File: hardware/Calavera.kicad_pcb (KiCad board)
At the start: 2 copper layers, 39.2 x 59.2 mm, 24 parts, among them Q1 DMN65D8L, SW1 SW_SPDT, U1 AT42QT1012, U2 LMV932

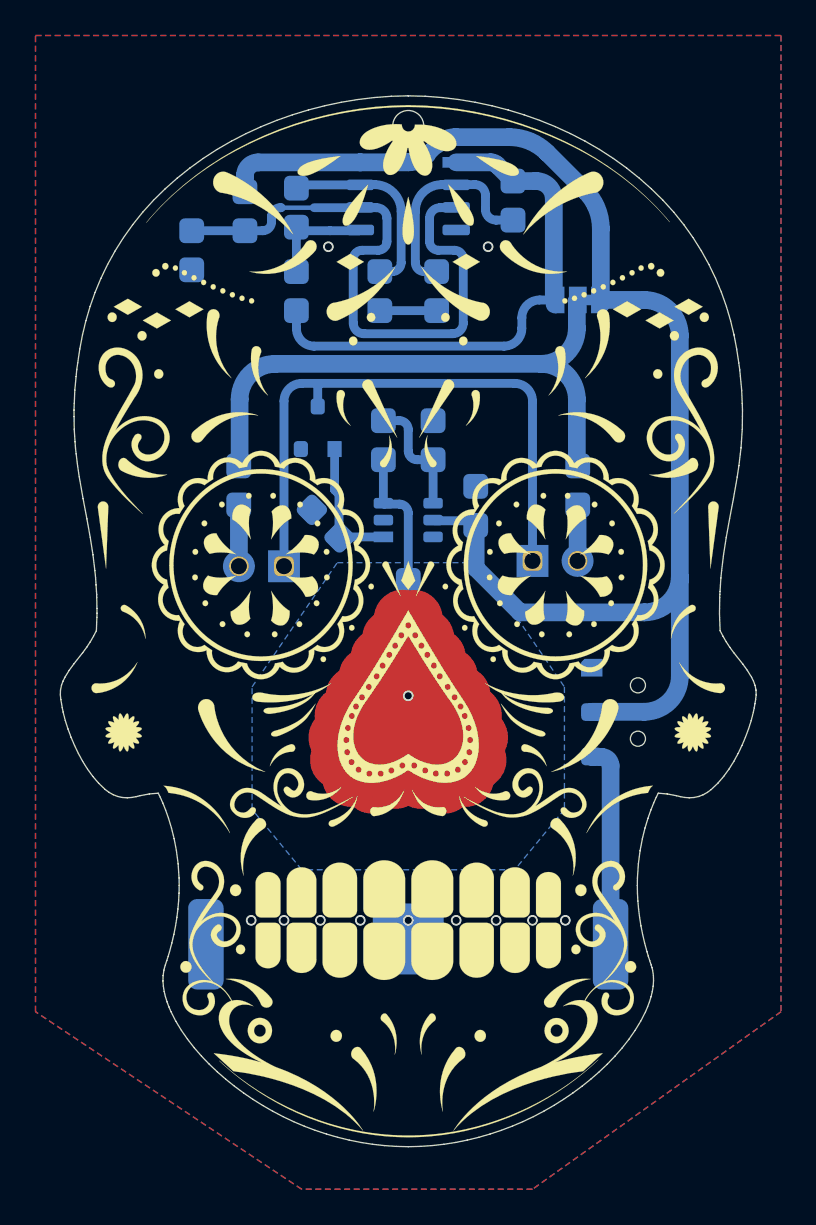
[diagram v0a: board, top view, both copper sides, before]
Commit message: 3D model behaves again
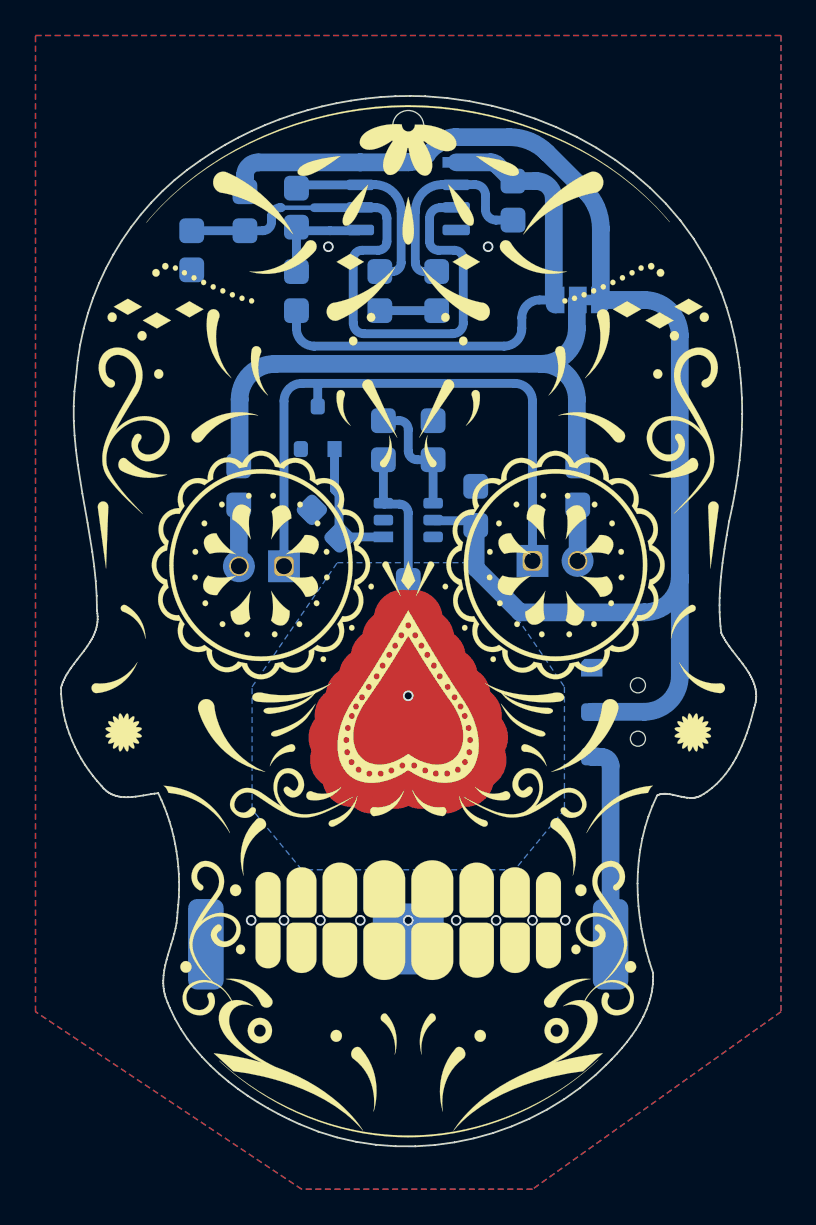
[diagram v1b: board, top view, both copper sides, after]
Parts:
- R8: value 1470Ω -> 1k5Ω
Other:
- outline, holes or cut-outs redrawn
